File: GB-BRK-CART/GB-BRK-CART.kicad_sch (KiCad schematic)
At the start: 7 parts

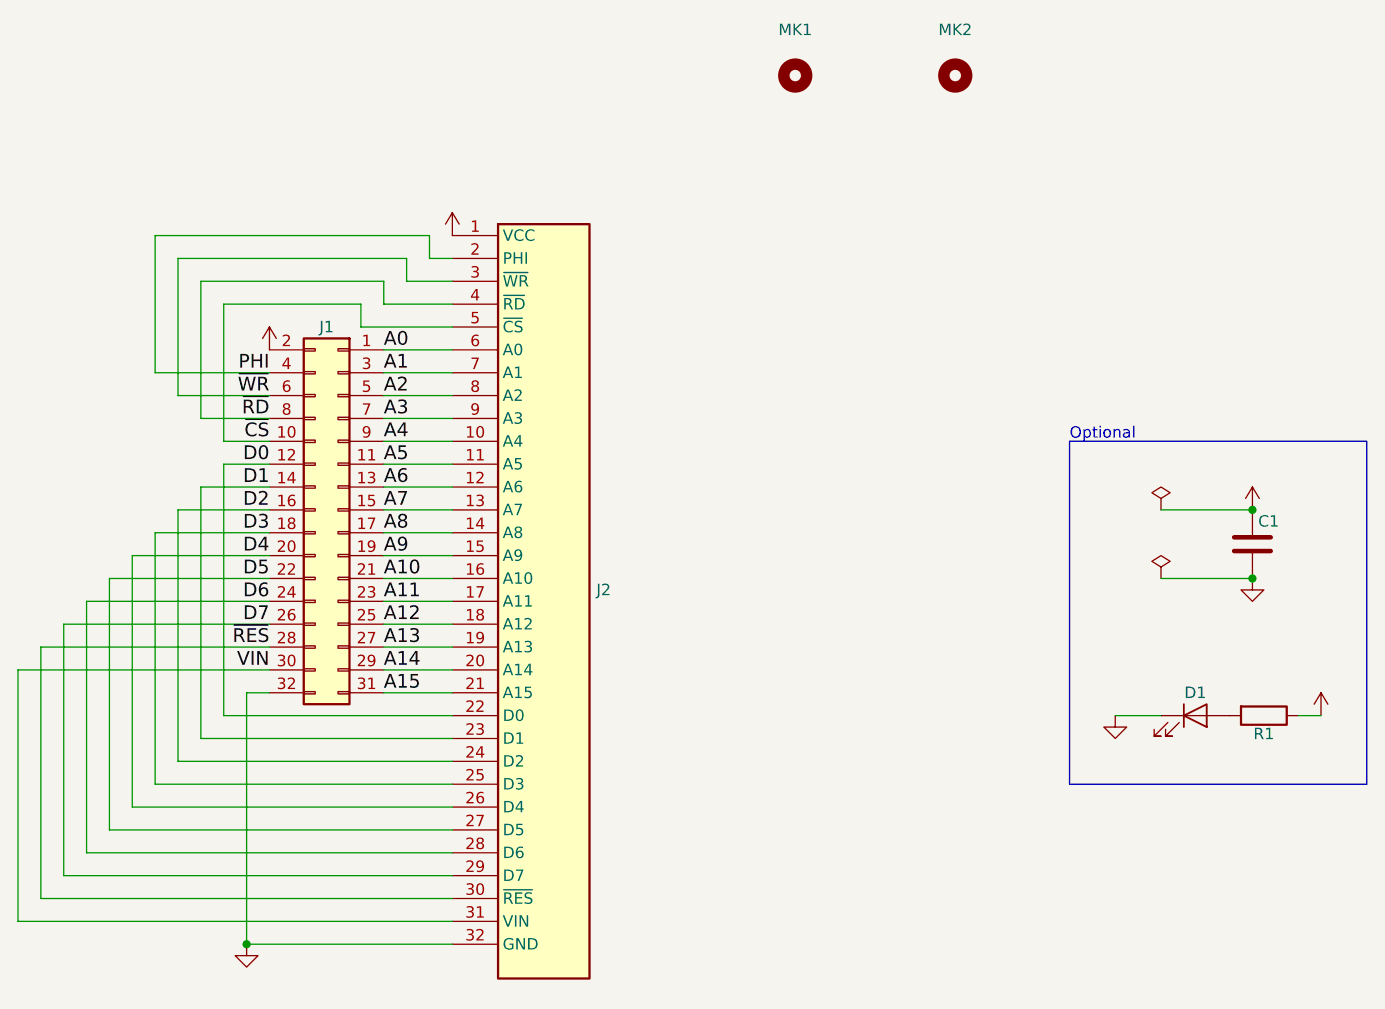
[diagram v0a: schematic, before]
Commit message: Upgrade projects to KiCad 7
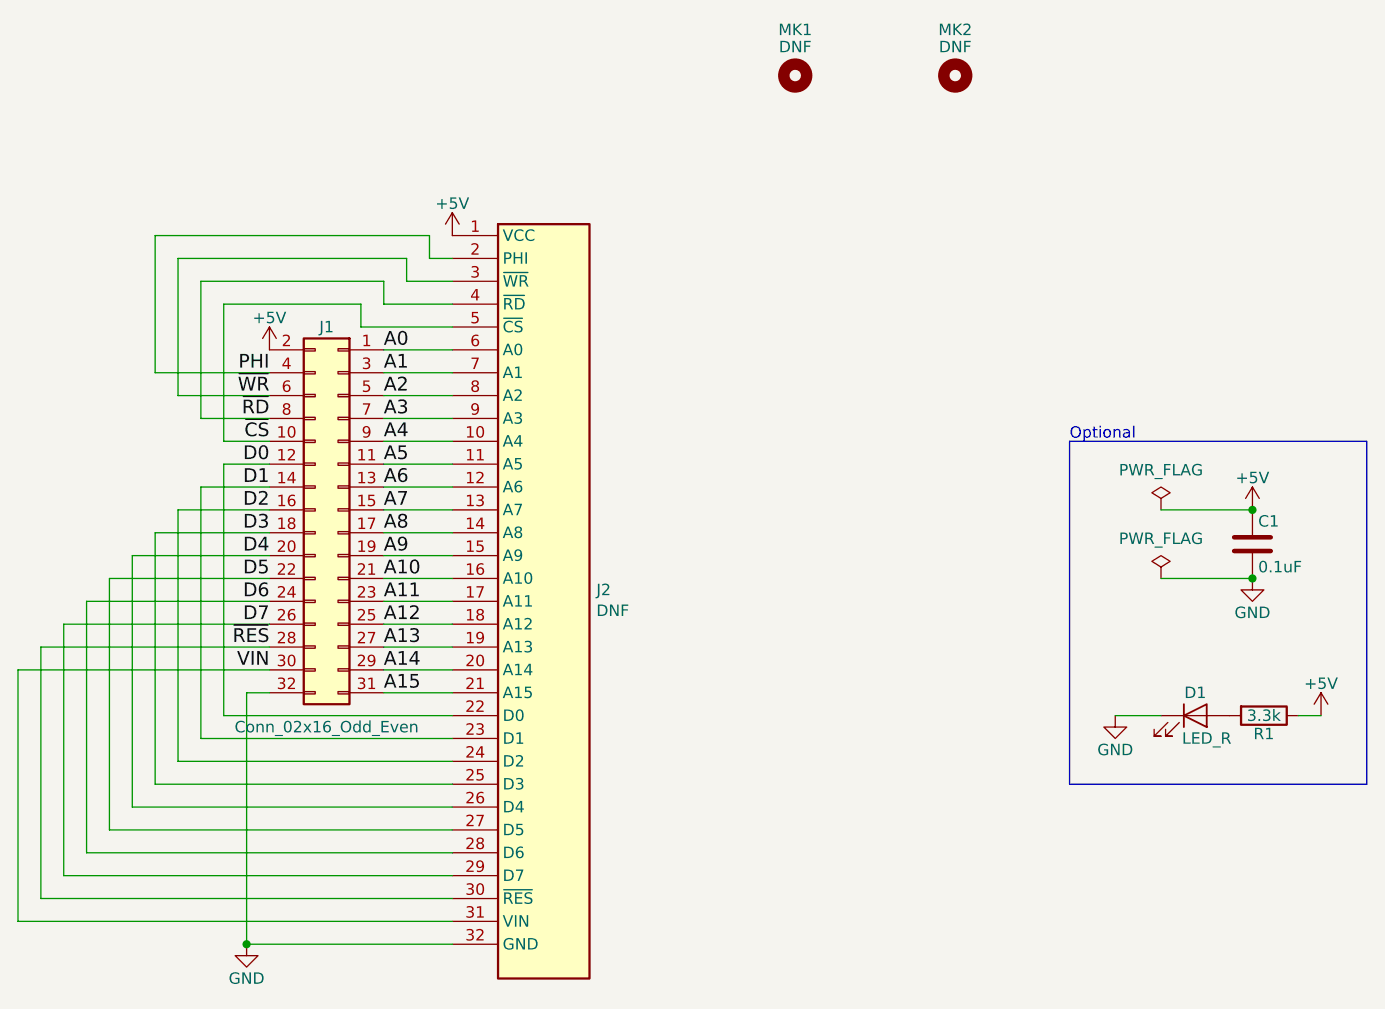
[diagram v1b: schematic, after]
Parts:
- C1: value (none) -> 0.1uF; footprint (none) -> Capacitor_SMD:C_0603_1608Metric
- D1: value (none) -> LED_R; footprint (none) -> LED_SMD:LED_0603_1608Metric
- J1: value (none) -> Conn_02x16_Odd_Even; footprint (none) -> Connector_PinHeader_2.54mm:PinHeader_2x16_P2.54mm_Vertical_SMD
- J2: value (none) -> DNF; footprint (none) -> Gekkio_Connector_PCBEdge:GameBoy_Cartridge_1x32_P1.50mm_Edge
- MK1: value (none) -> DNF; footprint (none) -> Gekkio_MountingHole:MountingHole_7.2mm
- MK2: value (none) -> DNF; footprint (none) -> Gekkio_MountingHole:MountingHole_2.3mm
- R1: value (none) -> 3.3k; footprint (none) -> Resistor_SMD:R_0603_1608Metric
